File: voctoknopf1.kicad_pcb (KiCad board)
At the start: 2 copper layers, 161.2 x 88.5 mm, 47 parts, among them SW1 MX_D, SW10 MX_D, SW11 MX_D, SW12 MX_D, SW2 MX_D, SW3 MX_D, SW4 MX_D, SW5 MX_D, SW6 MX_D, SW7 MX_D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

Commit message: dpi 89
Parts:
- added G***: LOGO, library:Untitled89, F.Cu at (91.5, 188.5)
- moved G*** 121.6 mm to (71.5, -53.5)
- moved SW1 1.25 mm to (30.2, 29.2)
- moved SW2 1.06 mm to (64.8, 29.2)
- moved SW4 1.03 mm to (26.0, 67.8)
- moved SW8 1.03 mm to (26.0, 93.8)
- moved SW6 0.79 mm to (77.8, 67.8)
- moved U3 0.79 mm to (126.0, 21.8)
- moved D2 0.75 mm to (126.2, 39.5)
- moved SW10 0.75 mm to (77.8, 93.5)
- moved SW3 0.56 mm to (99.5, 29.5)
- moved SW5 0.56 mm to (52.0, 67.8)
- moved SW7 0.56 mm to (103.5, 67.8)
- moved SW9 0.56 mm to (52.0, 93.8)
- moved D1 0.50 mm to (126.2, 31.2)
- moved SW11 0.25 mm to (103.8, 93.5)
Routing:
- net Net-(R2-Pad2): track 91.7 -> 99.0 mm
- net /GND: track 548.9 -> 555.3 mm
- net Net-(R14-Pad2): track 23.6 -> 27.7 mm
- net Net-(R4-Pad2): track 50.6 -> 53.3 mm
- net Net-(R21-Pad2): track 100.9 -> 103.5 mm
- net /5V: track 420.8 -> 423.1 mm
- net Net-(R18-Pad2): track 18.1 -> 20.0 mm
- net Net-(R23-Pad2): track 74.9 -> 76.2 mm
- net Net-(R1-Pad2): track 21.0 -> 22.1 mm
- net Net-(R11-Pad2): track 72.1 -> 73.1 mm
- net Net-(R22-Pad2): track 17.3 -> 18.1 mm
- net Net-(R6-Pad2): track 53.2 -> 52.5 mm
- net Net-(R12-Pad2): track 19.3 -> 18.7 mm
- net Net-(R16-Pad2): track 17.5 -> 17.0 mm
- net Net-(R20-Pad2): track 17.6 -> 18.1 mm
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- added copper zone on F.Cu, net (none)
- removed copper zone on F.Cu, net Net-(ARDUINO1-Pad16)

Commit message: ordentliche Proportionen
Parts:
- removed G***: LOGO, library:Untitled10
- removed G***: LOGO, library:Untitled89
- moved R6 2.14 mm to (111.2, 30.8)
- moved R5 1.82 mm to (111.5, 41.5)
- moved R7 0.79 mm to (117.2, 20.8)
- moved R8 0.50 mm to (117.8, 40.2)
- moved D2 0.35 mm to (126.0, 39.2)
- moved SW10 0.35 mm to (77.5, 93.8)
- moved SW11 0.35 mm to (103.5, 93.8)
- moved D1 0.25 mm to (126.0, 31.2)
- moved SW1 0.25 mm to (30.0, 29.2)
- moved SW3 0.25 mm to (99.5, 29.2)
- moved SW4 0.25 mm to (25.8, 67.8)
- moved SW6 0.25 mm to (77.5, 67.8)
- moved SW8 0.25 mm to (25.8, 93.8)
- moved SW9 0.25 mm to (51.8, 93.8)
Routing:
- net /GND: track 555.3 -> 557.1 mm
- net Net-(R5-Pad1): track 46.9 -> 47.6 mm
- net Net-(R6-Pad2): track 52.5 -> 51.9 mm

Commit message: pbc done
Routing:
- net /GND: track 557.1 -> 555.7 mm
- net Net-(R15-Pad2): track 37.6 -> 38.2 mm
- net Net-(R10-Pad2): track 20.6 -> 21.2 mm
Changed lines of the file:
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@@
     (thickness 1.6)
     (drawings 7)
-    (tracks 570)
+    (tracks 569)
     (zones 0)
     (modules 46)
@@
   (segment (start 72.5 95.5) (end 73.25 96.25) (width 0.25) (layer B.Cu) (net 1))
   (segment (start 73.25 96.25) (end 79.98 96.25) (width 0.25) (layer B.Cu) (net 1))
-  (segment (start 71.5 94.5) (end 72.5 95.5) (width 0.25) (layer B.Cu) (net 1))
   (segment (start 95.5 81) (end 99.89 81) (width 0.25) (layer B.Cu) (net 1))
   (segment (start 99.89 81) (end 107.31 72.83) (width 0.25) (layer B.Cu) (net 1) (status 20))
@@
   (segment (start 45 46.5) (end 36.25 55.25) (width 0.25) (layer F.Cu) (net 16))
   (segment (start 36.25 55.25) (end 31.75 55.25) (width 0.25) (layer F.Cu) (net 16))
-  (segment (start 20 64.75) (end 19.25 65.5) (width 0.25) (layer F.Cu) (net 17))
-  (segment (start 24.13 60.62) (end 20 64.75) (width 0.25) (layer F.Cu) (net 17))
-  (segment (start 22.19 72.83) (end 20 69.89) (width 0.25) (layer F.Cu) (net 17) (status 20))
-  (segment (start 24.13 60.62) (end 24.13 55.25) (width 0.25) (layer F.Cu) (net 17))
-  (segment (start 20 69.5) (end 20 69.89) (width 0.25) (layer F.Cu) (net 17))
-  (segment (start 19.25 68.75) (end 20 69.5) (width 0.25) (layer F.Cu) (net 17))
-  (segment (start 19.25 65.5) (end 19.25 68.75) (width 0.25) (layer F.Cu) (net 17))
+  (segment (start 21.94 72.83) (end 21.83 72.83) (width 0.25) (layer F.Cu) (net 17))
+  (segment (start 21.83 72.83) (end 18.75 69.75) (width 0.25) (layer F.Cu) (net 17))
+  (segment (start 18.75 69.75) (end 18.75 65.5) (width 0.25) (layer F.Cu) (net 17))
+  (segment (start 18.75 65.5) (end 24.13 60.12) (width 0.25) (layer F.Cu) (net 17))
+  (segment (start 24.13 60.12) (end 24.13 55.25) (width 0.25) (layer F.Cu) (net 17))
   (via (at 62.75 49) (size 0.6) (drill 0.4) (layers F.Cu B.Cu) (net 18))
   (segment (start 45 49) (end 45 49.25) (width 0.25) (layer B.Cu) (net 18))
@@
   (segment (start 71.5 69.89) (end 71.75 70.19123) (width 0.25) (layer B.Cu) (net 23) (status 20))
   (segment (start 71.75 70.19123) (end 73.94 72.83) (width 0.25) (layer B.Cu) (net 23) (status 20))
-  (segment (start 80.75 71.25) (end 80.25 71.25) (width 0.25) (layer F.Cu) (net 24))
-  (segment (start 75 67.160256) (end 75 69) (width 0.25) (layer F.Cu) (net 24))
+  (segment (start 74.5 68.5) (end 74.5 69) (width 0.25) (layer F.Cu) (net 24))
+  (segment (start 74.5 67) (end 74.5 68.5) (width 0.25) (layer F.Cu) (net 24))
+  (segment (start 73.69 66.19) (end 74.5 67) (width 0.25) (layer F.Cu) (net 24) (status 400000))
+  (segment (start 76.75 71.25) (end 77.5 71.25) (width 0.25) (layer F.Cu) (net 24))
+  (segment (start 74.5 69) (end 76.75 71.25) (width 0.25) (layer F.Cu) (net 24))
+  (segment (start 73.69 65.21) (end 73.69 66.19) (width 0.25) (layer F.Cu) (net 24) (status C00000))
+  (segment (start 79.75 71.25) (end 77.5 71.25) (width 0.25) (layer F.Cu) (net 24))
+  (segment (start 79.75 71.25) (end 80.75 71.25) (width 0.25) (layer F.Cu) (net 24))
+  (segment (start 80.75 71.25) (end 90.13 71.25) (width 0.25) (layer F.Cu) (net 24))
   (segment (start 90.13 71.25) (end 91 72.12) (width 0.25) (layer F.Cu) (net 24))
-  (segment (start 80.75 71.25) (end 90.13 71.25) (width 0.25) (layer F.Cu) (net 24))
-  (segment (start 78 72) (end 80 72) (width 0.25) (layer F.Cu) (net 24))
-  (segment (start 75.5 69.5) (end 78 72) (width 0.25) (layer F.Cu) (net 24))
-  (segment (start 75.5 69.5) (end 75 69) (width 0.25) (layer F.Cu) (net 24))
-  (segment (start 80 71.5) (end 80 72) (width 0.25) (layer F.Cu) (net 24))
-  (segment (start 80.25 71.25) (end 80 71.5) (width 0.25) (layer F.Cu) (net 24))
-  (segment (start 73.94 66.44) (end 75 67.160256) (width 0.25) (layer F.Cu) (net 24) (status 10))
-  (segment (start 75 67.160256) (end 75 67.25) (width 0.25) (layer F.Cu) (net 24))
-  (segment (start 75 67.25) (end 75 67.160256) (width 0.25) (layer F.Cu) (net 24))
+  (segment (start 77.5 71.25) (end 77.25 71.25) (width 0.25) (layer F.Cu) (net 24))
   (segment (start 73.94 65.21) (end 73.94 66.44) (width 0.25) (layer F.Cu) (net 24) (status 30))
   (segment (start 73.94 65.21) (end 73.94 64.69) (width 0.25) (layer F.Cu) (net 24) (status 30))
@@
   (segment (start 54.37 84.13) (end 48.19 90.06) (width 0.25) (layer F.Cu) (net 33) (status 20))
   (segment (start 48.19 90.06) (end 48.19 91.21) (width 0.25) (layer F.Cu) (net 33) (status 30))
-  (segment (start 91 88.5) (end 103 88.5) (width 0.25) (layer F.Cu) (net 34))
-  (segment (start 124.95 87) (end 126.25 88.3) (width 0.25) (layer F.Cu) (net 34))
+  (segment (start 104.75 90.25) (end 105 90.5) (width 0.25) (layer F.Cu) (net 34))
+  (segment (start 103 88.5) (end 104.75 90.25) (width 0.25) (layer F.Cu) (net 34))
+  (segment (start 108.75 90.25) (end 112 87) (width 0.25) (layer F.Cu) (net 34))
   (segment (start 112 87) (end 124.95 87) (width 0.25) (layer F.Cu) (net 34))
-  (segment (start 108.75 90.25) (end 112 87) (width 0.25) (layer F.Cu) (net 34))
-  (segment (start 104.75 90.25) (end 108.75 90.25) (width 0.25) (layer F.Cu) (net 34))
-  (segment (start 103 88.5) (end 104.75 90.25) (width 0.25) (layer F.Cu) (net 34))
+  (segment (start 126.25 88.3) (end 124.95 87) (width 0.25) (layer F.Cu) (net 34))
+  (segment (start 103 88.5) (end 91 88.5) (width 0.25) (layer F.Cu) (net 34))
+  (segment (start 108.5 90.5) (end 108.75 90.25) (width 0.25) (layer F.Cu) (net 34))
+  (segment (start 108.25 90.5) (end 108.5 90.5) (width 0.25) (layer F.Cu) (net 34))
+  (segment (start 105 90.5) (end 108.25 90.5) (width 0.25) (layer F.Cu) (net 34))
   (segment (start 73.94 98.58) (end 78.67 98.58) (width 0.25) (layer F.Cu) (net 35) (status 10))
   (segment (start 81.13 96.12) (end 91 96.12) (width 0.25) (layer F.Cu) (net 35))

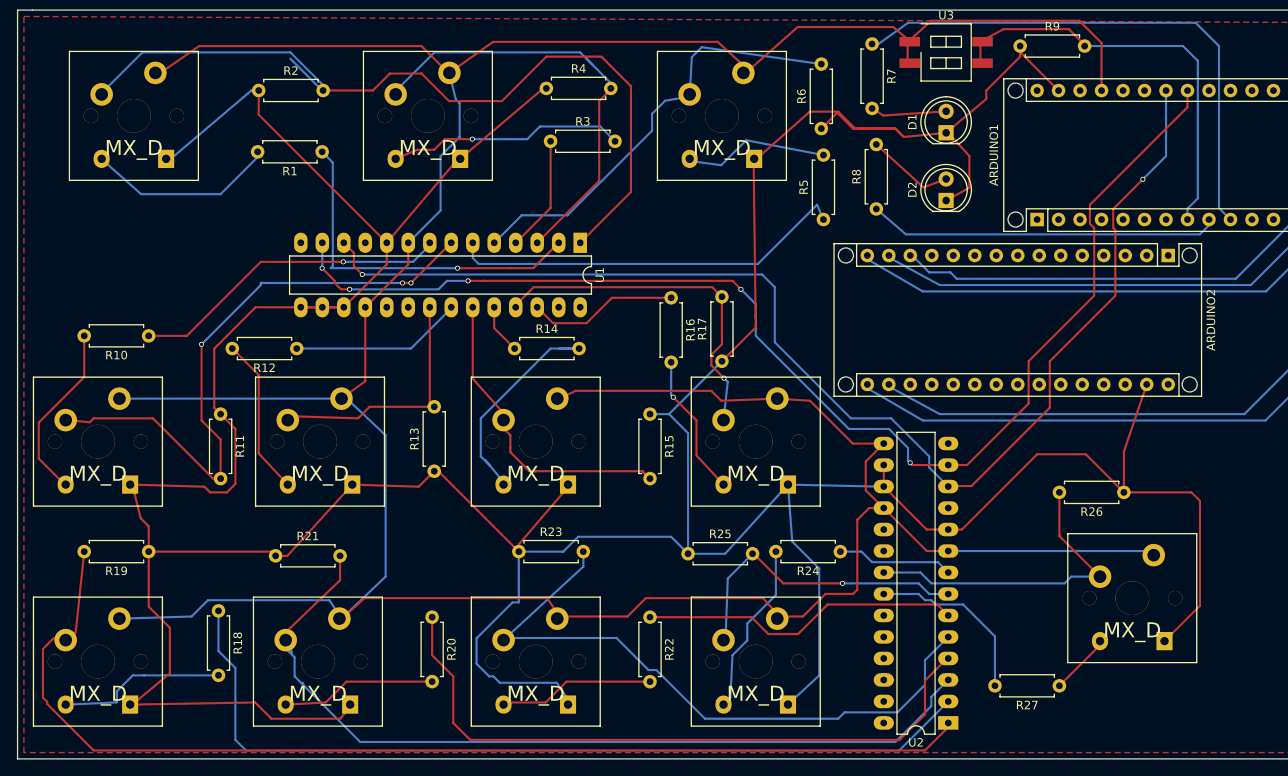
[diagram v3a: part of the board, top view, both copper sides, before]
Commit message: pcb bug free (so it says), and new freecad file
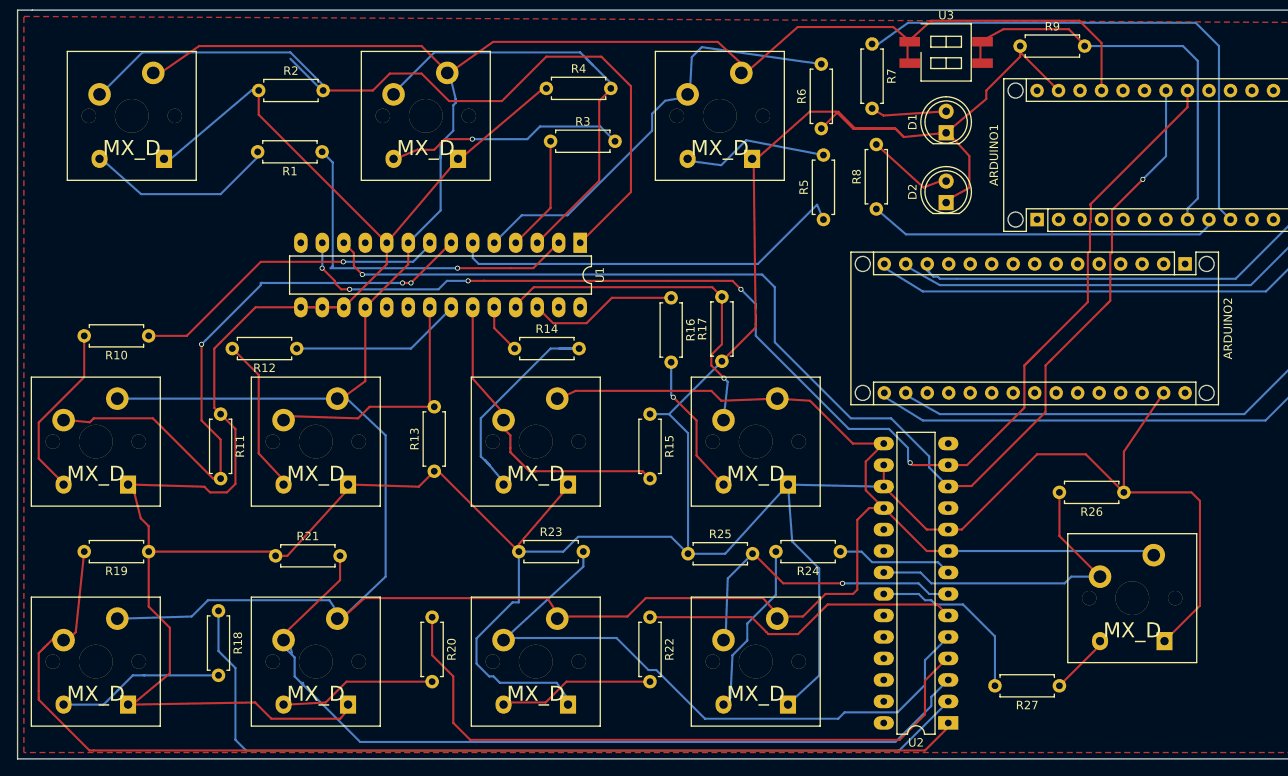
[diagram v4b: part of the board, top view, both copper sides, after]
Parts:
- moved ARDUINO2 2.24 mm to (154.2, 46.8)
- moved SW5 0.50 mm to (51.5, 67.8)
- moved D2 0.25 mm to (126.0, 39.5)
- moved SW1 0.25 mm to (29.8, 29.2)
- moved SW2 0.25 mm to (64.5, 29.2)
- moved SW4 0.25 mm to (25.5, 67.8)
- moved SW8 0.25 mm to (25.5, 93.8)
- moved SW9 0.25 mm to (51.5, 93.8)
- moved SW3 0.25 mm to (99.3, 29.2)
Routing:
- net Net-(ARDUINO1-Pad17): track 87.9 -> 85.7 mm
- net Net-(ARDUINO1-Pad14): track 54.8 -> 52.6 mm
- net Net-(ARDUINO1-Pad16): track 94.7 -> 92.4 mm
- net Net-(ARDUINO1-Pad15): track 60.6 -> 58.4 mm
- net Net-(ARDUINO1-Pad23): track 148.7 -> 150.9 mm
- net Net-(R19-Pad2): track 131.5 -> 132.6 mm
- net Net-(ARDUINO1-Pad13): track 49.5 -> 48.8 mm
- net Net-(ARDUINO1-Pad24): track 148.1 -> 148.7 mm

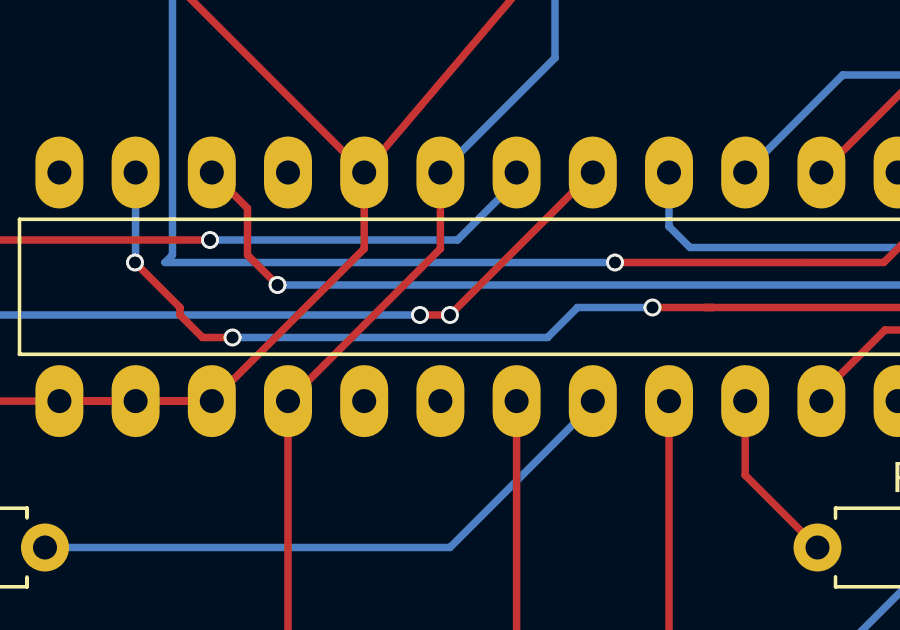
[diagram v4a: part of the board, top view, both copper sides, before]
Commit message: removed superfluous via
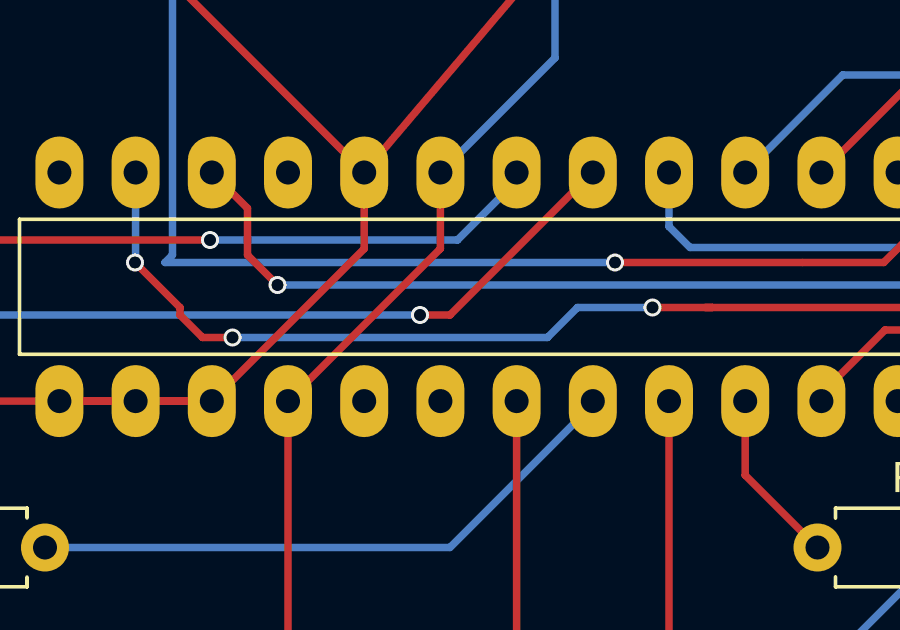
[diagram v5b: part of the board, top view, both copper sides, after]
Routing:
- net Net-(R11-Pad2): vias 3 -> 2
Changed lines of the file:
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@@
     (thickness 1.6)
     (drawings 7)
-    (tracks 593)
+    (tracks 592)
     (zones 0)
     (modules 46)
@@
     (visible_elements FFFFFF7F)
     (pcbplotparams
-      (layerselection 0x01060_80000001)
+      (layerselection 0x3ffff_80000001)
       (usegerberextensions false)
       (excludeedgelayer true)
@@
   (segment (start 18.75 65.5) (end 24.13 60.12) (width 0.25) (layer F.Cu) (net 17))
   (segment (start 24.13 60.12) (end 24.13 55.25) (width 0.25) (layer F.Cu) (net 17))
-  (via (at 62.75 49) (size 0.6) (drill 0.4) (layers F.Cu B.Cu) (net 18))
   (segment (start 45 49) (end 45 49.25) (width 0.25) (layer B.Cu) (net 18))
   (segment (start 40.25 67.5) (end 40.25 72.12) (width 0.25) (layer F.Cu) (net 18))
